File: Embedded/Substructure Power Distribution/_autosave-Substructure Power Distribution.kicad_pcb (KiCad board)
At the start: 4 copper layers, 55 x 20 mm, 56 parts, among them J1 S JST, J2 D0 FFC, J3 D1 FFC, J4 S Pins A, J5 S Pins B, Q1 CSD17577Q5A, Q2 CSD17577Q5A, Q3 CSD17573Q5B, Q4 CSD17577Q5A, U1 LM5176PWP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

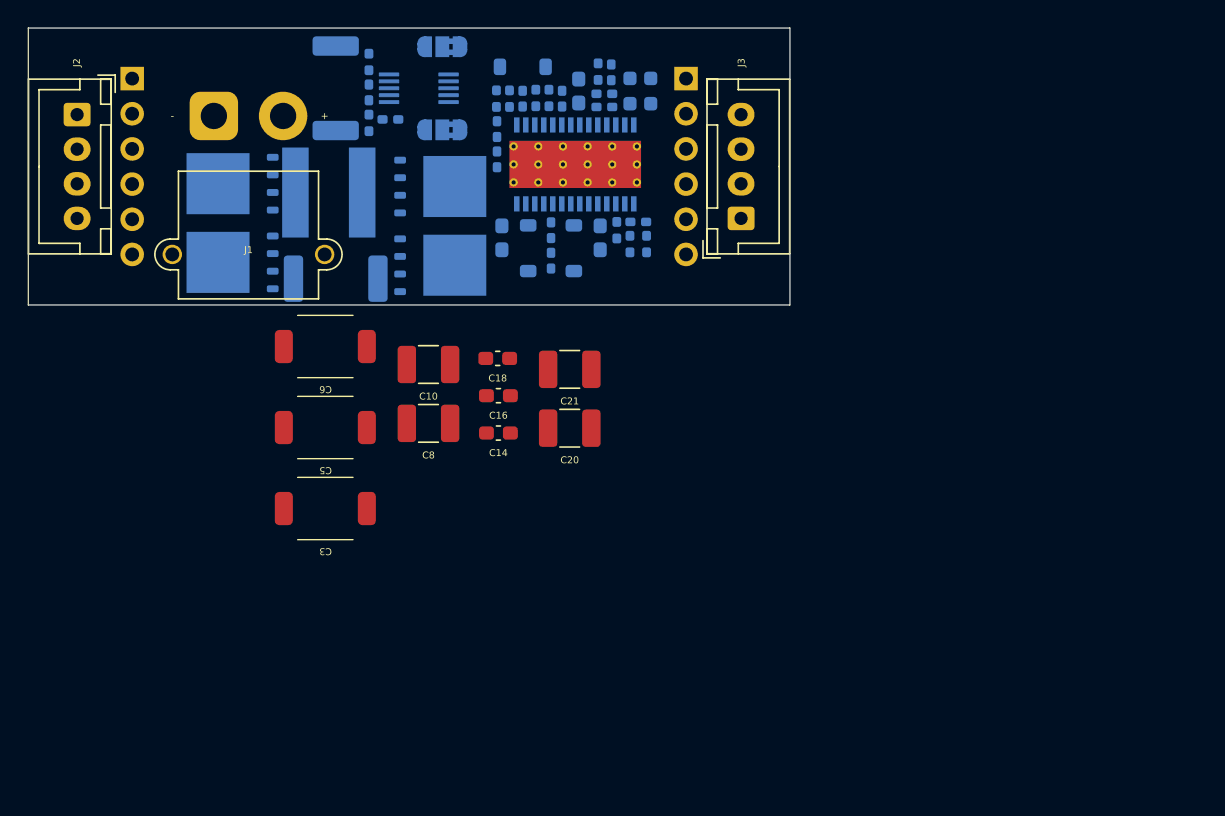
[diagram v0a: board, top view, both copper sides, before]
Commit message: Modified Thyristor (Replaced component)
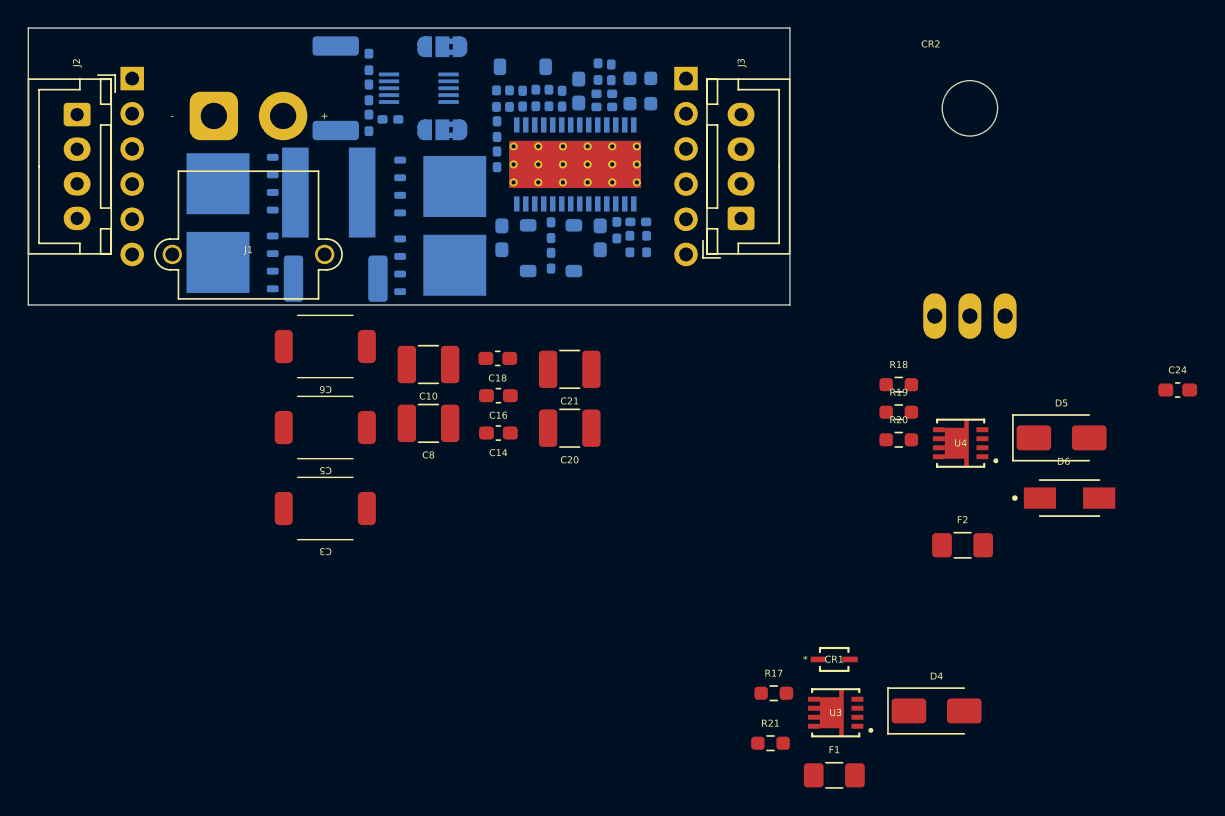
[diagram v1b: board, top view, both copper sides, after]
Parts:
- added C24: 0.1uF, Capacitor_SMD:C_0603_1608Metric_Pad1.08x0.95mm_HandSolder, F.Cu at (155.5, 131.1)
- added CR1: BZT52C6V2S-7-F, Zener Diode:SOD323_DIO, F.Cu at (130.7, 150.6)
- added CR2: TYN625RG, Thyristor TYN:TO-220, F.Cu at (140.5, 125.8)
- added D4: SMAJ26A, Diode_SMD:D_SMA, F.Cu at (138.1, 154.3)
- added D5: SMAJ26A, Diode_SMD:D_SMA, F.Cu at (147.1, 134.6)
- added D6: 1SMA5919BT3G, Zener Diode:DIOM5226X220N, F.Cu at (147.7, 138.9)
- added F1: Fuse, Fuse:Fuse_1206_3216Metric_Pad1.42x1.75mm_HandSolder, F.Cu at (130.7, 159.0)
- added F2: Fuse, Fuse:Fuse_1206_3216Metric_Pad1.42x1.75mm_HandSolder, F.Cu at (140.0, 142.4)
- added R17: 100K, Resistor_SMD:R_0603_1608Metric_Pad0.98x0.95mm_HandSolder, F.Cu at (126.3, 153.0)
- added R18: 10K, Resistor_SMD:R_0603_1608Metric_Pad0.98x0.95mm_HandSolder, F.Cu at (135.4, 130.8)
- added R19: 10K, Resistor_SMD:R_0603_1608Metric_Pad0.98x0.95mm_HandSolder, F.Cu at (135.4, 132.7)
- added R20: 1M, Resistor_SMD:R_0603_1608Metric_Pad0.98x0.95mm_HandSolder, F.Cu at (135.4, 134.7)
- added R21: 1M, Resistor_SMD:R_0603_1608Metric_Pad0.98x0.95mm_HandSolder, F.Cu at (126.1, 156.7)
- added U3: SI7111EDN-T1-GE3, P Channel Mosfet:MOSFET_0DN-T1-GE3_VIS, F.Cu at (130.8, 154.4)
- added U4: SI7111EDN-T1-GE3, P Channel Mosfet:MOSFET_0DN-T1-GE3_VIS, F.Cu at (139.8, 135.0)
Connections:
- C14 pad 1: +5V -> +5VP
- C16 pad 1: +5V -> +5VP
- C18 pad 1: +5V -> +5VP
- C20 pad 1: +5V -> +5VP
- C21 pad 1: +5V -> +5VP
- Q3 pad 5: +5V -> +5VP
- R12 pad 1: +5V -> +5VP
- R14 pad 1: +RAWVS -> +RAWVK
- R15 pad 1: +RAWVS -> +RAWVK
- U1 pad 12: +5V -> +5VP
